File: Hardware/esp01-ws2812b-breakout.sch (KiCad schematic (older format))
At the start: 21 parts, among them J1 Screw_Terminal_01x02, J2 Screw_Terminal_01x04, J3 Conn_01x03_Male, Q1 IRFS4127, Q2 IRFS4127, U1 LM1117-3.3, U2 ESP-01v090, U3 DS18B20

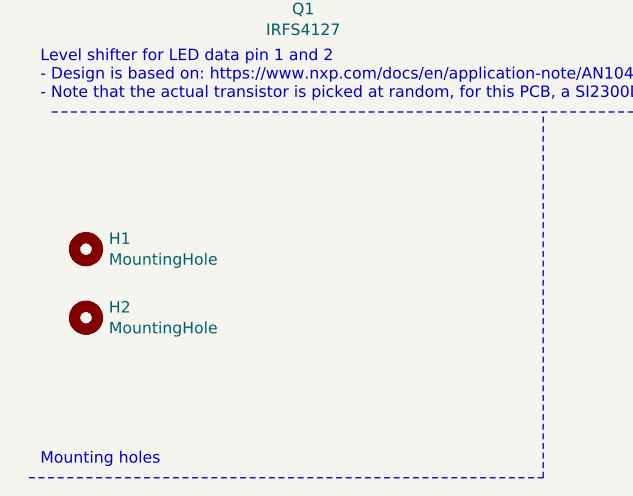
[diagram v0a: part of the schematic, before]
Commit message: Finalized PCB layout, added PDF+PNG
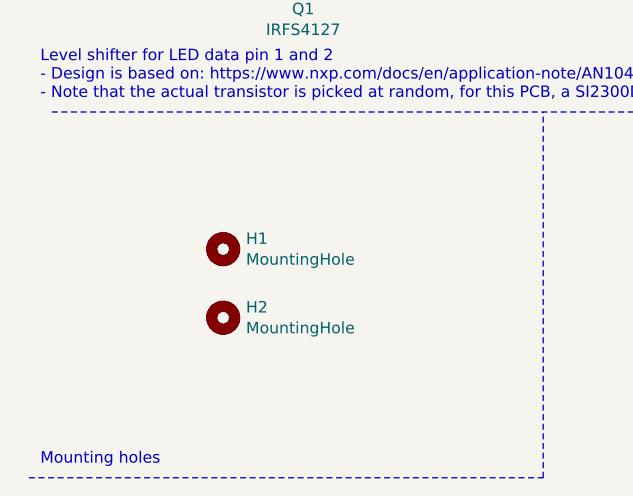
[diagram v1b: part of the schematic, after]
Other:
- moved on the sheet: H1, H2
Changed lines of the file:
@@
 Sheet 1 1
 Title "ESP-01 5V RGB LED Breakout Board"
-Date "2020-12-21"
+Date "2020-12-29"
 Rev ""
 Comp ""
@@
 L Mechanical:MountingHole H1
 U 1 1 5FE31388
-P 750 4350
-F 0 "H1" H 850 4396 50  0000 L CNN
-F 1 "MountingHole" H 850 4305 50  0000 L CNN
-F 2 "MountingHole:MountingHole_2.2mm_M2" H 750 4350 50  0001 C CNN
-F 3 "~" H 750 4350 50  0001 C CNN
-	1    750  4350
+P 1350 4350
+F 0 "H1" H 1450 4396 50  0000 L CNN
+F 1 "MountingHole" H 1450 4305 50  0000 L CNN
+F 2 "MountingHole:MountingHole_2.2mm_M2" H 1350 4350 50  0001 C CNN
+F 3 "~" H 1350 4350 50  0001 C CNN
+	1    1350 4350
 	1    0    0    -1
 $EndComp
@@
 L Mechanical:MountingHole H2
 U 1 1 5FE31DB5
-P 750 4650
-F 0 "H2" H 850 4696 50  0000 L CNN
-F 1 "MountingHole" H 850 4605 50  0000 L CNN
-F 2 "MountingHole:MountingHole_2.2mm_M2" H 750 4650 50  0001 C CNN
-F 3 "~" H 750 4650 50  0001 C CNN
-	1    750  4650
-	1    0    0    -1
-$EndComp
+P 1350 4650
+F 0 "H2" H 1450 4696 50  0000 L CNN
+F 1 "MountingHole" H 1450 4605 50  0000 L CNN
+F 2 "MountingHole:MountingHole_2.2mm_M2" H 1350 4650 50  0001 C CNN
+F 3 "~" H 1350 4650 50  0001 C CNN
+	1    1350 4650
+	1    0    0    -1
+$EndComp

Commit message: Checked an finalized designs for production
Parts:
- Q1, Q2: symbol Transistor_FET:IRFS4127 -> esp01-ws2812b-breakout-rescue:IRFS4127-Transistor_FET
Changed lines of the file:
@@
 	2250 1350 2550 1350
 $Comp
-L Transistor_FET:IRFS4127 Q1
+L esp01-ws2812b-breakout-rescue:IRFS4127-Transistor_FET Q1
 U 1 1 5FE1865D
 P 1700 3050
@@
 	2000 3150 2100 3150
 $Comp
-L Transistor_FET:IRFS4127 Q2
+L esp01-ws2812b-breakout-rescue:IRFS4127-Transistor_FET Q2
 U 1 1 5FE26590
 P 3950 3050

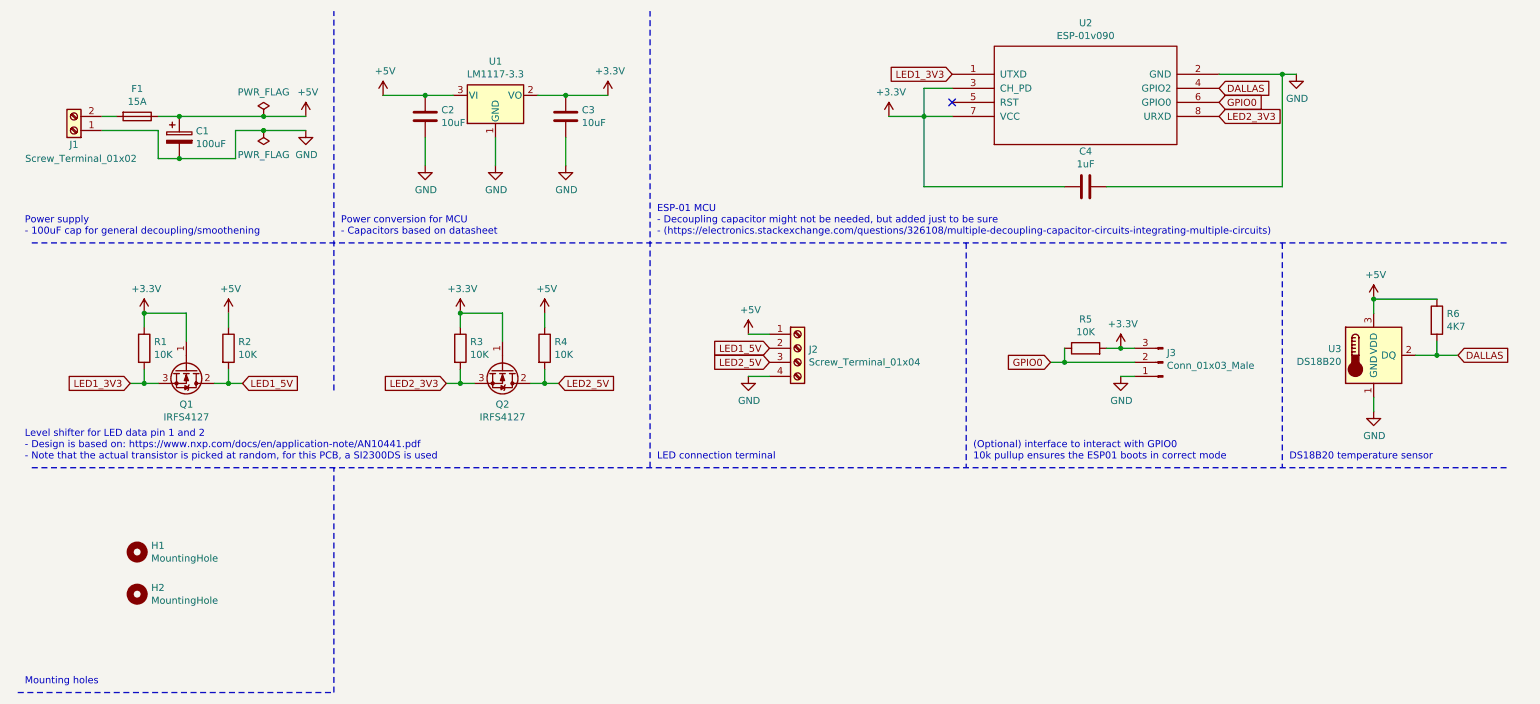
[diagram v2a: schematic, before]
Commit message: Removed second LED channel
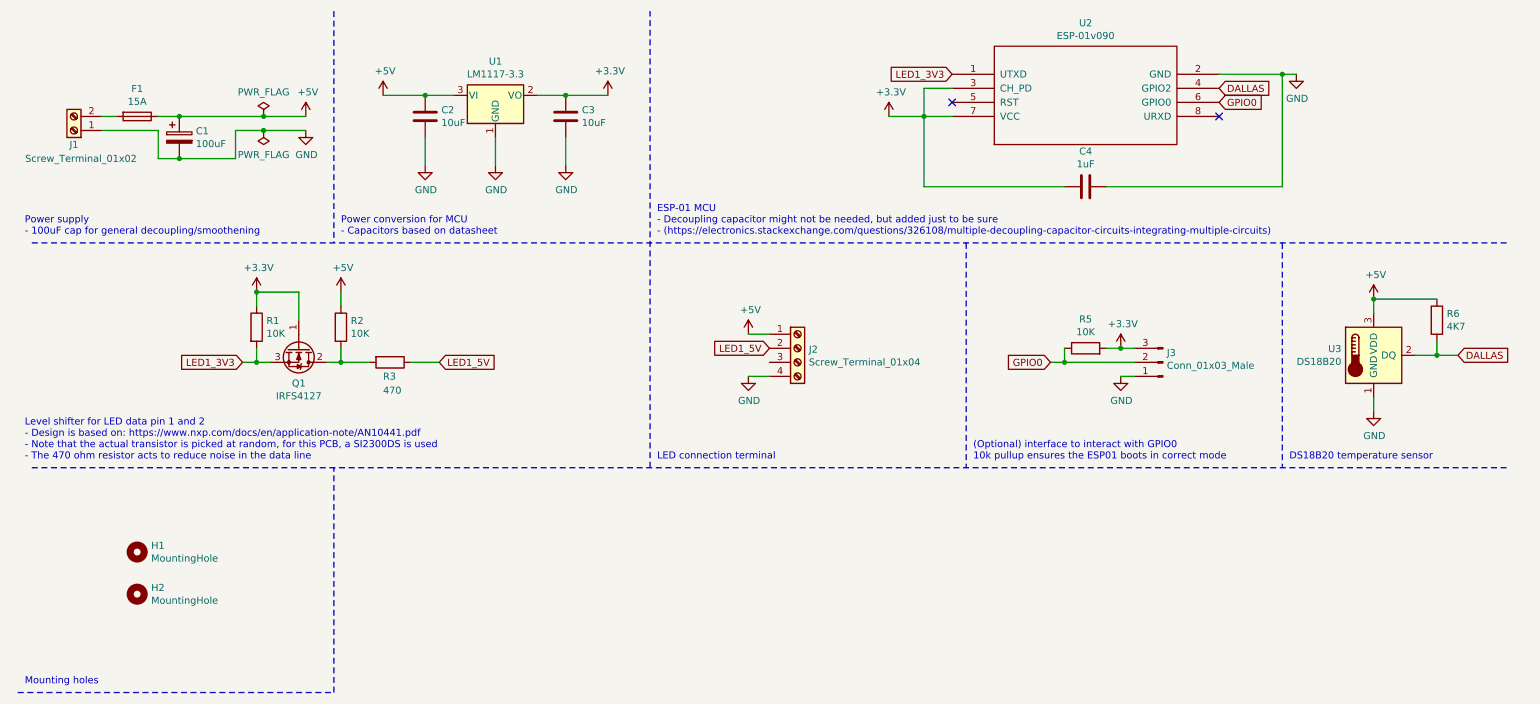
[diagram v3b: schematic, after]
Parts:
- removed Q2: IRFS4127, Custom Mosfets:SOT-23_DS-REVERSED, symbol esp01-ws2812b-breakout-rescue:IRFS4127-Transistor_FET
- removed R4: 10K, Resistor_SMD:R_0805_2012Metric_Pad1.20x1.40mm_HandSolder, symbol Device:R
- R3: value 10K -> 470
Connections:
- net +3V3: no longer R3.1
- net LED1_5V: now also R3.1; no longer Q1.2 (D), R2.2
- net LED2_3V3: no longer names the net of U2.8 (URXD)
- net LED2_3V3: no longer R3.2
- net LED2_5V: no longer names the net of J2.3 (Pin_3)
- new net: Q1.2 (D), R2.2, R3.2
- no-connect marks 1 -> 2
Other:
- note added: "Level shifter for LED data pin 1 and 2 \n- Design is based on: https://www.nxp.com/docs/en/application-note/AN10441.pdf\n- Note that the actual transistor is picked at random, for this PCB, a SI2300DS is used\n- The 470 ohm resistor acts to reduce noise in the data line"
- note removed: "Level shifter for LED data pin 1 and 2 \n- Design is based on: https://www.nxp.com/docs/en/application-note/AN10441.pdf\n- Note that the actual transistor is picked at random, for this PCB, a SI2300DS is used"
- moved on the sheet: Q1, R1, R2

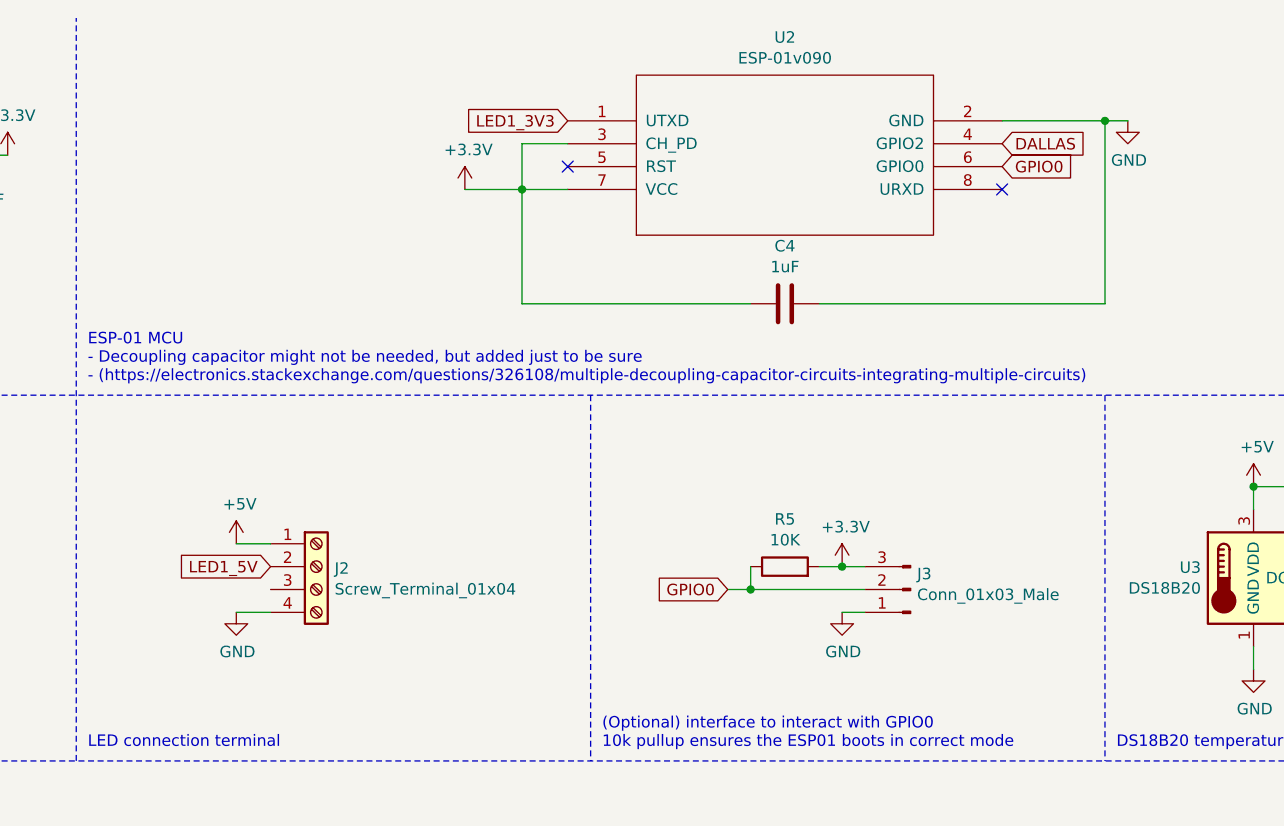
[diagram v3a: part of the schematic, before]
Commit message: Updated to correct LED pin
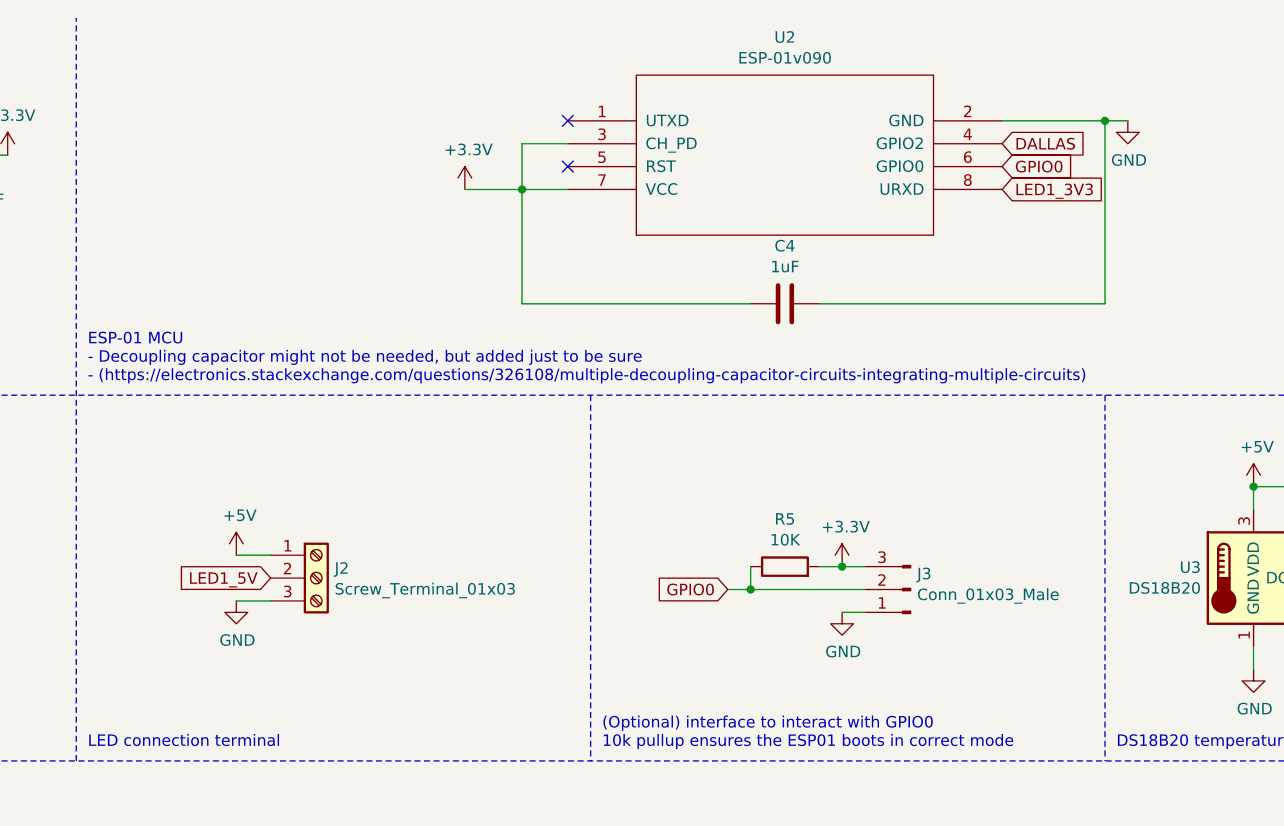
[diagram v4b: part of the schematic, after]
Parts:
- removed J2: Screw_Terminal_01x04, Custom Terminals:0104-blue-terminal, symbol Connector:Screw_Terminal_01x04
- added J2: Screw_Terminal_01x03, symbol Connector:Screw_Terminal_01x03
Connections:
- net +5V: now also J2.1 (Pin_1)
- net GND: now also J2.3 (Pin_3)
- net LED1_3V3: now also U2.8 (URXD); no longer U2.1 (UTXD)
- net LED1_5V: now also J2.2 (Pin_2)
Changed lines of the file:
@@
 Text GLabel 9050 1050 2    50   Input ~ 0
 DALLAS
-Text GLabel 7150 950  0    50   Input ~ 0
+Text GLabel 9050 1250 2    50   Input ~ 0
 LED1_3V3
 Wire Wire Line
@@
 L power:+5V #PWR012
 U 1 1 5FE128C5
-P 5700 2800
-F 0 "#PWR012" H 5700 2650 50  0001 C CNN
-F 1 "+5V" H 5715 2973 50  0000 C CNN
-F 2 "" H 5700 2800 50  0001 C CNN
-F 3 "" H 5700 2800 50  0001 C CNN
-	1    5700 2800
+P 5700 2850
+F 0 "#PWR012" H 5700 2700 50  0001 C CNN
+F 1 "+5V" H 5715 3023 50  0000 C CNN
+F 2 "" H 5700 2850 50  0001 C CNN
+F 3 "" H 5700 2850 50  0001 C CNN
+	1    5700 2850
 	1    0    0    -1
 $EndComp
@@
 L power:GND #PWR013
 U 1 1 5FE130D4
-P 5700 3100
-F 0 "#PWR013" H 5700 2850 50  0001 C CNN
-F 1 "GND" H 5705 2927 50  0000 C CNN
-F 2 "" H 5700 3100 50  0001 C CNN
-F 3 "" H 5700 3100 50  0001 C CNN
-	1    5700 3100
+P 5700 3050
+F 0 "#PWR013" H 5700 2800 50  0001 C CNN
+F 1 "GND" H 5705 2877 50  0000 C CNN
+F 2 "" H 5700 3050 50  0001 C CNN
+F 3 "" H 5700 3050 50  0001 C CNN
+	1    5700 3050
 	1    0    0    -1
 $EndComp
 Wire Notes Line
 	600  3750 11100 3750
-Text GLabel 5850 2900 0    50   Input ~ 0
+Text GLabel 5850 2950 0    50   Input ~ 0
 LED1_5V
 $Comp
@@
 	10600 2550 10150 2550
 Connection ~ 10150 2550
-$Comp
-L Connector:Screw_Terminal_01x04 J2
-U 1 1 5FE369E1
-P 6050 2900
-F 0 "J2" H 6130 2892 50  0000 L CNN
-F 1 "Screw_Terminal_01x04" H 6130 2801 50  0000 L CNN
-F 2 "Custom Terminals:0104-blue-terminal" H 6050 2900 50  0001 C CNN
-F 3 "~" H 6050 2900 50  0001 C CNN
-	1    6050 2900
-	1    0    0    -1
-$EndComp
-Wire Wire Line
-	5850 2800 5700 2800
-Wire Wire Line
-	5700 3100 5850 3100
+Wire Wire Line
+	5850 2850 5700 2850
 $Comp
 L power:PWR_FLAG #FLG01
@@
 	-1   0    0    1
 $EndComp
-NoConn ~ 9050 1250
+NoConn ~ 7150 950
 Wire Wire Line
 	3300 3000 3500 3000
@@
 Text Notes 550  2100 0    50   ~ 0
 Power supply\n- 100uF cap for general decoupling/smoothening
+$Comp
+L Connector:Screw_Terminal_01x03 J2
+U 1 1 61A8EA8C
+P 6050 2950
+F 0 "J2" H 6130 2992 50  0000 L CNN
+F 1 "Screw_Terminal_01x03" H 6130 2901 50  0000 L CNN
+F 2 "" H 6050 2950 50  0001 C CNN
+F 3 "~" H 6050 2950 50  0001 C CNN
+	1    6050 2950
+	1    0    0    -1
+$EndComp
+Wire Wire Line
+	5700 3050 5850 3050
 $EndSCHEMATC

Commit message: Started re-doing the PCB layout
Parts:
- J2: footprint (none) -> custom_terminals:0103-blue-terminal
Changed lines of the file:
@@
 F 0 "J2" H 6130 2992 50  0000 L CNN
 F 1 "Screw_Terminal_01x03" H 6130 2901 50  0000 L CNN
-F 2 "" H 6050 2950 50  0001 C CNN
+F 2 "custom_terminals:0103-blue-terminal" H 6050 2950 50  0001 C CNN
 F 3 "~" H 6050 2950 50  0001 C CNN
 	1    6050 2950

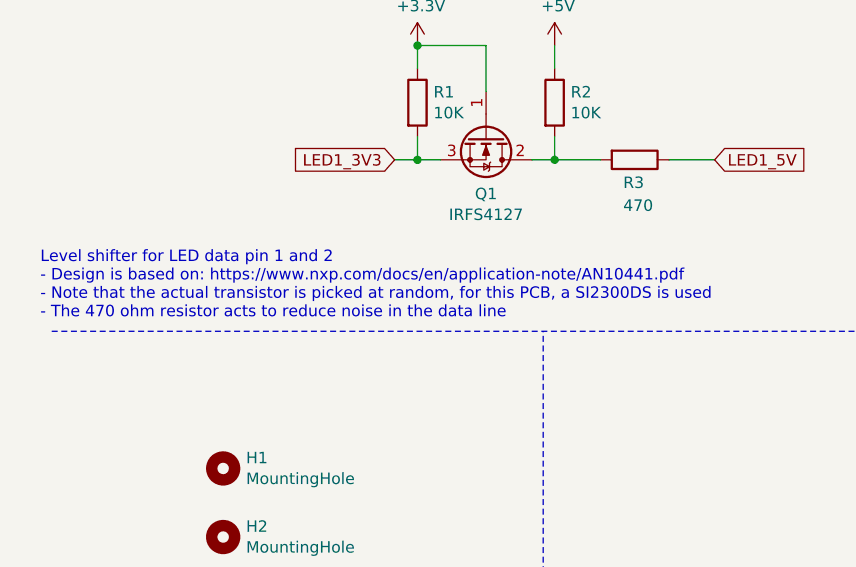
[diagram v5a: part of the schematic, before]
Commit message: Updated schematic export, finished PCB design
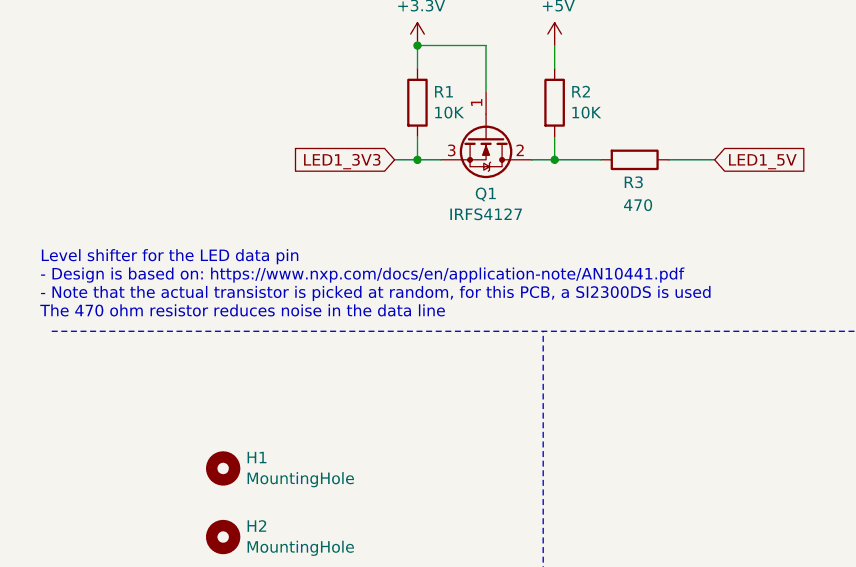
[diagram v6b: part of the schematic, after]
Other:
- note added: "Level shifter for the LED data pin\n- Design is based on: https://www.nxp.com/docs/en/application-note/AN10441.pdf\n- Note that the actual transistor is picked at random, for this PCB, a SI2300DS is used\nThe 470 ohm resistor reduces noise in the data line"
- note removed: "Level shifter for LED data pin 1 and 2 \n- Design is based on: https://www.nxp.com/docs/en/application-note/AN10441.pdf\n- Note that the actual transistor is picked at random, for this PCB, a SI2300DS is used\n- The 470 ohm resistor acts to reduce noise in the data line"
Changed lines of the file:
@@
 	2250 1350 2550 1350
 Text Notes 550  3700 0    50   ~ 0
-Level shifter for LED data pin 1 and 2 \n- Design is based on: https://www.nxp.com/docs/en/application-note/AN10441.pdf\n- Note that the actual transistor is picked at random, for this PCB, a SI2300DS is used\n- The 470 ohm resistor acts to reduce noise in the data line
+Level shifter for the LED data pin\n- Design is based on: https://www.nxp.com/docs/en/application-note/AN10441.pdf\n- Note that the actual transistor is picked at random, for this PCB, a SI2300DS is used\nThe 470 ohm resistor reduces noise in the data line
 Wire Notes Line
 	5000 3750 5000 500
